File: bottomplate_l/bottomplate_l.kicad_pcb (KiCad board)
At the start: 2 copper layers, 133.3 x 104.8 mm, 28 parts, among them SW1 SW_PUSH, SW10 SW_PUSH, SW11 SW_PUSH, SW12 SW_PUSH, SW13 SW_PUSH, SW14 SW_PUSH, SW15 SW_PUSH, SW16 SW_PUSH, SW17 SW_PUSH, SW18 SW_PUSH, SW19 SW_PUSH, SW2 SW_PUSH, SW20 SW_PUSH, SW21 SW_PUSH, SW22 SW_PUSH, SW3 SW_PUSH, SW4 SW_PUSH, SW5 SW_PUSH, SW6 SW_PUSH, SW7 SW_PUSH, SW8 SW_PUSH, SW9 SW_PUSH

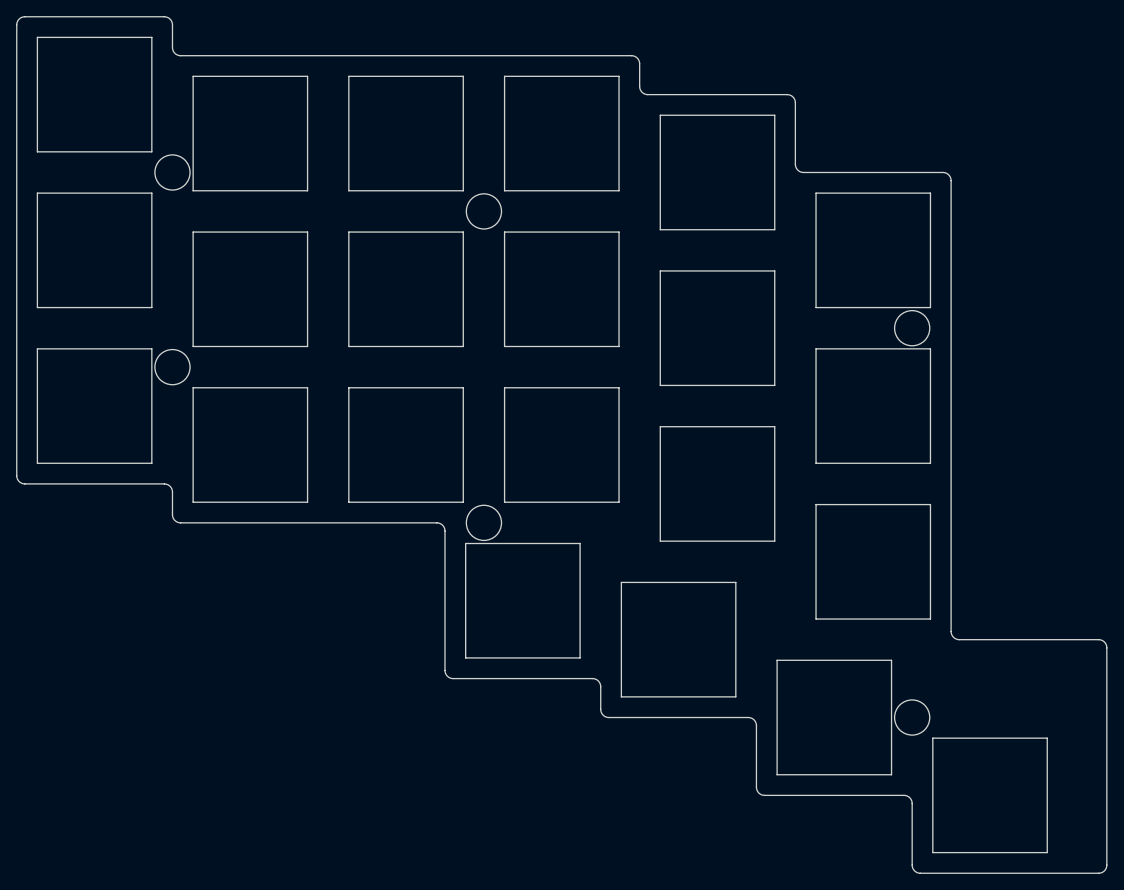
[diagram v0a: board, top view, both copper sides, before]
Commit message: added bottomplate
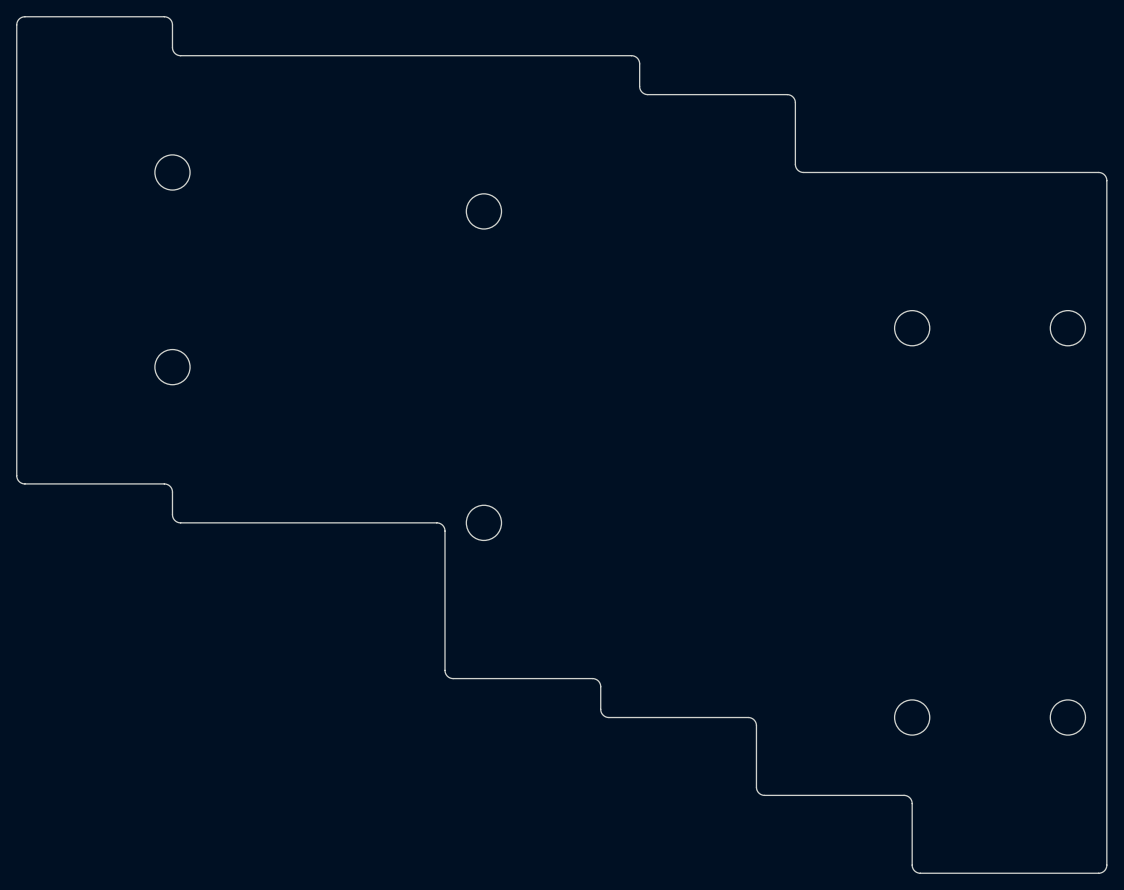
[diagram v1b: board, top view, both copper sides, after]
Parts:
- removed SW1, SW10, SW11, SW12, SW13, SW14, SW15, SW16, SW17, SW18, SW19, SW2, SW20, SW21, SW22, SW3, SW4, SW5, SW6, SW7, SW8, SW9: SW_PUSH, kbd:SW_Hole
- added Ref**: Val**, kbd:M2_HOLE_v2, F.Cu at (147.6, 107.2)
- added Ref**: Val**, kbd:M2_HOLE_v2, F.Cu at (147.6, 59.5)
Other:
- outline, holes or cut-outs redrawn

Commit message: added gnd mask
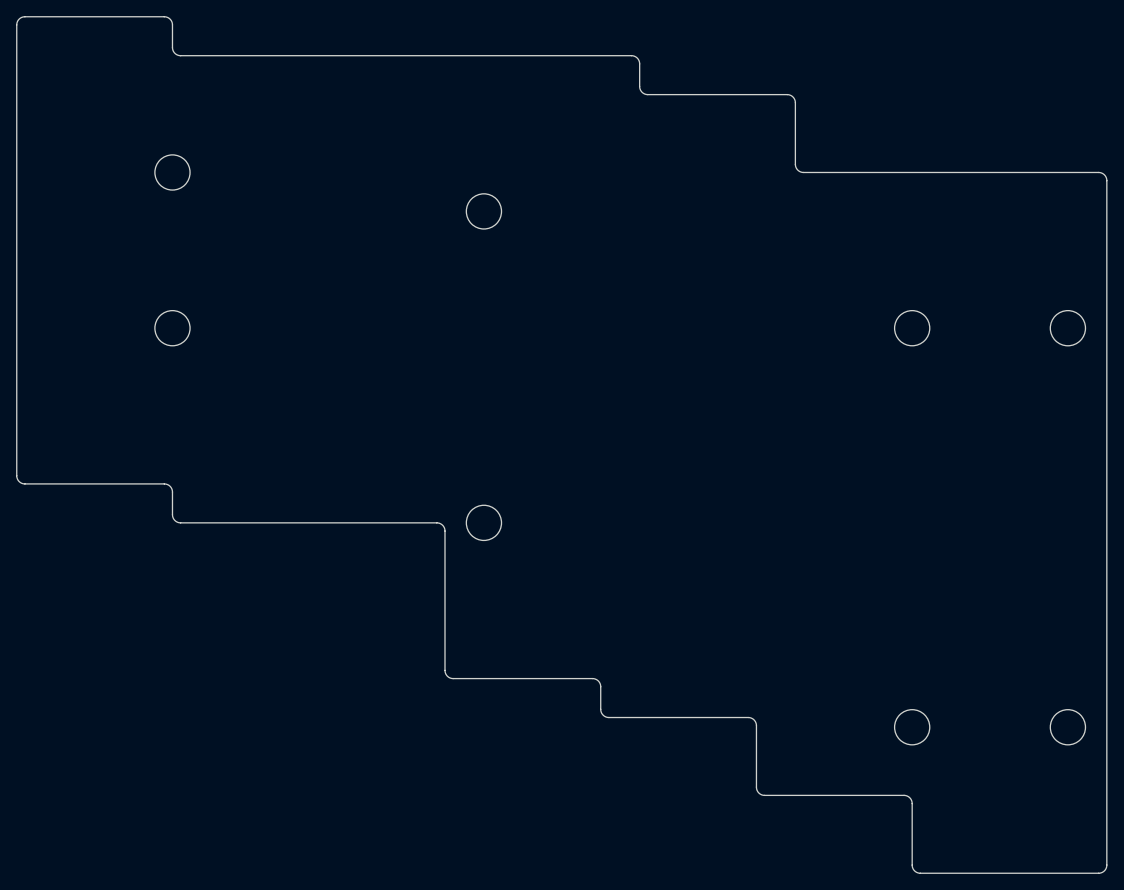
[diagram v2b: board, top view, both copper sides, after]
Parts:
- moved Ref** 4.76 mm to (38.1, 59.5)
- moved Ref** 1.19 mm to (147.6, 108.3)
- moved Ref** 1.19 mm to (128.6, 108.3)
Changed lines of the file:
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@@
   (net 0 "")
   (footprint "kbd:M2_HOLE_v2" (layer "F.Cu")
-    (at 147.6375 107.15625)
+    (at 147.6375 108.346875)
     (descr "Mounting Hole 2.2mm, no annular, M2")
     (tags "mounting hole 2.2mm no annular m2")
@@
   )
   (footprint "kbd:M2_HOLE_v2" (layer "F.Cu")
-    (at 38.1 64.29375)
+    (at 38.1 59.53125)
     (descr "Mounting Hole 2.2mm, no annular, M2")
     (tags "mounting hole 2.2mm no annular m2")
@@
   )
   (footprint "kbd:M2_HOLE_v2" (layer "F.Cu")
-    (at 128.5875 107.15625)
+    (at 128.5875 108.346875)
     (descr "Mounting Hole 2.2mm, no annular, M2")
     (tags "mounting hole 2.2mm no annular m2")

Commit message: fixed hole size
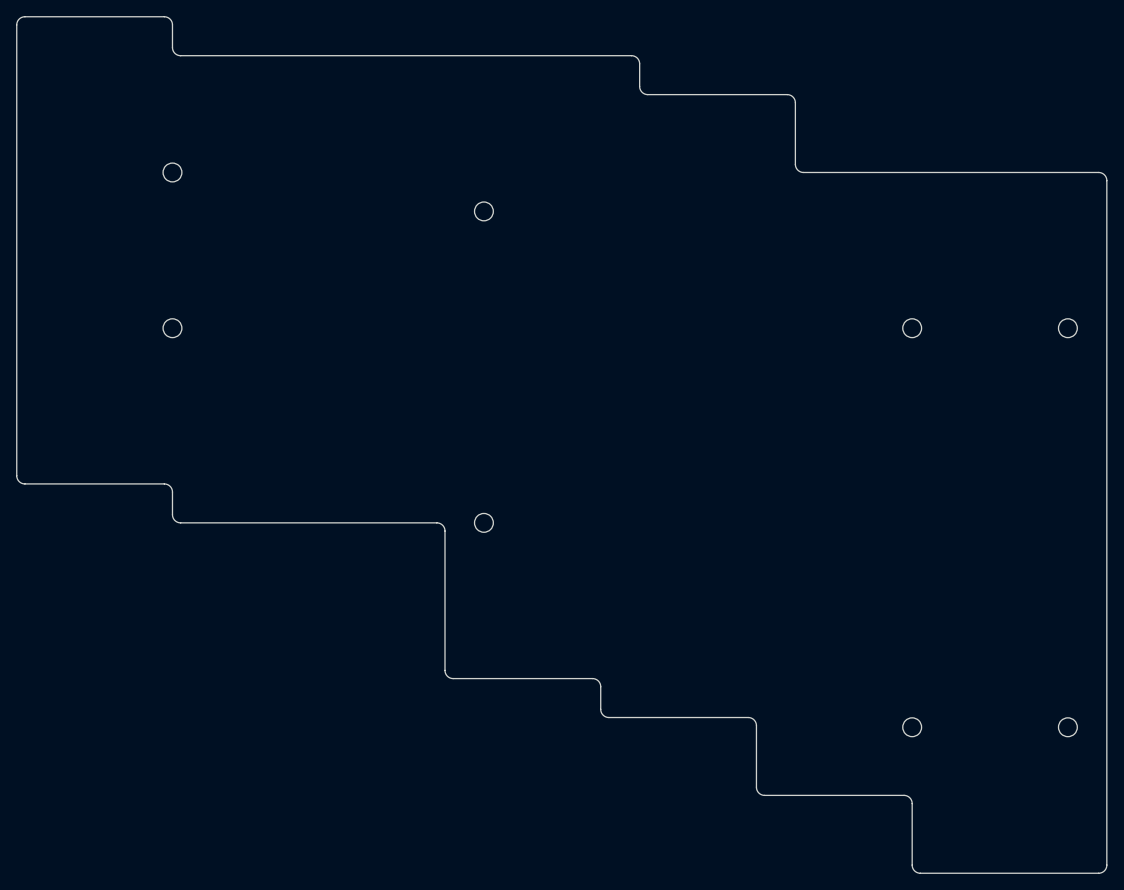
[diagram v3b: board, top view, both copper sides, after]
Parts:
- Ref** (x8): footprint kbd:M2_HOLE_v2 -> kbd:thread_m2
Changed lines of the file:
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@@
   )
   (net 0 "")
-  (footprint "kbd:M2_HOLE_v2" (layer "F.Cu")
+  (footprint "kbd:thread_m2" (layer "F.Cu")
     (at 147.6375 108.346875)
     (descr "Mounting Hole 2.2mm, no annular, M2")
@@
         (effects (font (size 1 1) (thickness 0.15)))
     )
-    (pad "" np_thru_hole circle (at 0 0) (size 4.3 4.3) (drill 4.3) (layers "*.Cu" "*.Mask"))
+    (pad "" np_thru_hole circle (at 0 0) (size 2.3 2.3) (drill 2.3) (layers "*.Cu" "*.Mask"))
   )
-  (footprint "kbd:M2_HOLE_v2" (layer "F.Cu")
+  (footprint "kbd:thread_m2" (layer "F.Cu")
     (at 76.2 45.24375)
     (descr "Mounting Hole 2.2mm, no annular, M2")
@@
         (effects (font (size 1 1) (thickness 0.15)))
     )
-    (pad "" np_thru_hole circle (at 0 0) (size 4.3 4.3) (drill 4.3) (layers "*.Cu" "*.Mask"))
+    (pad "" np_thru_hole circle (at 0 0) (size 2.3 2.3) (drill 2.3) (layers "*.Cu" "*.Mask"))
   )
-  (footprint "kbd:M2_HOLE_v2" (layer "F.Cu")
+  (footprint "kbd:thread_m2" (layer "F.Cu")
     (at 147.6375 59.53125)
     (descr "Mounting Hole 2.2mm, no annular, M2")
@@
         (effects (font (size 1 1) (thickness 0.15)))
     )
-    (pad "" np_thru_hole circle (at 0 0) (size 4.3 4.3) (drill 4.3) (layers "*.Cu" "*.Mask"))
+    (pad "" np_thru_hole circle (at 0 0) (size 2.3 2.3) (drill 2.3) (layers "*.Cu" "*.Mask"))
   )
-  (footprint "kbd:M2_HOLE_v2" (layer "F.Cu")
+  (footprint "kbd:thread_m2" (layer "F.Cu")
     (at 128.5875 59.53125)
     (descr "Mounting Hole 2.2mm, no annular, M2")
@@
         (effects (font (size 1 1) (thickness 0.15)))
     )
-    (pad "" np_thru_hole circle (at 0 0) (size 4.3 4.3) (drill 4.3) (layers "*.Cu" "*.Mask"))
+    (pad "" np_thru_hole circle (at 0 0) (size 2.3 2.3) (drill 2.3) (layers "*.Cu" "*.Mask"))
   )
-  (footprint "kbd:M2_HOLE_v2" (layer "F.Cu")
+  (footprint "kbd:thread_m2" (layer "F.Cu")
     (at 38.1 59.53125)
     (descr "Mounting Hole 2.2mm, no annular, M2")
@@
         (effects (font (size 1 1) (thickness 0.15)))
     )
-    (pad "" np_thru_hole circle (at 0 0) (size 4.3 4.3) (drill 4.3) (layers "*.Cu" "*.Mask"))
+    (pad "" np_thru_hole circle (at 0 0) (size 2.3 2.3) (drill 2.3) (layers "*.Cu" "*.Mask"))
   )
-  (footprint "kbd:M2_HOLE_v2" (layer "F.Cu")
+  (footprint "kbd:thread_m2" (layer "F.Cu")
     (at 38.1 40.48125)
     (descr "Mounting Hole 2.2mm, no annular, M2")
@@
         (effects (font (size 1 1) (thickness 0.15)))
     )
-    (pad "" np_thru_hole circle (at 0 0) (size 4.3 4.3) (drill 4.3) (layers "*.Cu" "*.Mask"))
+    (pad "" np_thru_hole circle (at 0 0) (size 2.3 2.3) (drill 2.3) (layers "*.Cu" "*.Mask"))
   )
-  (footprint "kbd:M2_HOLE_v2" (layer "F.Cu")
+  (footprint "kbd:thread_m2" (layer "F.Cu")
     (at 128.5875 108.346875)
     (descr "Mounting Hole 2.2mm, no annular, M2")
@@
         (effects (font (size 1 1) (thickness 0.15)))
     )
-    (pad "" np_thru_hole circle (at 0 0) (size 4.3 4.3) (drill 4.3) (layers "*.Cu" "*.Mask"))
+    (pad "" np_thru_hole circle (at 0 0) (size 2.3 2.3) (drill 2.3) (layers "*.Cu" "*.Mask"))
   )
-  (footprint "kbd:M2_HOLE_v2" (layer "F.Cu")
+  (footprint "kbd:thread_m2" (layer "F.Cu")
     (at 76.2 83.34375)
     (descr "Mounting Hole 2.2mm, no annular, M2")
@@
         (effects (font (size 1 1) (thickness 0.15)))
     )
-    (pad "" np_thru_hole circle (at 0 0) (size 4.3 4.3) (drill 4.3) (layers "*.Cu" "*.Mask"))
+    (pad "" np_thru_hole circle (at 0 0) (size 2.3 2.3) (drill 2.3) (layers "*.Cu" "*.Mask"))
   )
   (gr_line (start 173.974915 57.00545) (end 173.974915 43.00615)
